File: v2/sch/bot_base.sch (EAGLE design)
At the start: 35 parts, among them K1 SKQGADE010, Q0 QWIIC_RIGHT_ANGLE, U1 ESP32-C3-MINI-1-N4, U2 AP7370-33SA (or MCP1703T-3302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, U4 LGS4084HB5

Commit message: routing almost finished
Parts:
- removed JUMPER_LIPO_CHG: NO-FIT, solder_jumper:WIRELINK2
- removed K1: SKQGADE010, Seeed-OPL-Button:SMD-SWITCH-TOP-260GF(4P-D5.2MM)
- added K2: DTSM-62K-S-V-T/R, Seeed-OPL-Button:SMD-SWITCH-TACTILE-SPST-NO(4P-D6.0MM)
- added R10: 10k, rcl:R-EU_R0603
- added SERVO: (no value), pinhead-2:PINHD-1X03_2.54-S
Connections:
- removed net N$2: JUMPER_LIPO_CHG.1, U4.BAT
- removed net N$7: K1.A0, U1.IO9
- new net BOOT: K2.A0, U1.IO9
- new net MOTOR1A_LV: U$3.INA, U1.IO4
- new net MOTOR1B_LV: U$3.INB, U1.IO7
- new net MOTOR2A_LV: U$4.INA, U1.IO6
- new net MOTOR2B_LV: U$4.INB, U1.IO5
- net +5V: now also SERVO.2, U$9.P$1
- net BUTTONS: now also R10.2
- net GND: now also C3.1, C4.1, K2.B0, SERVO.1, U$5.4; no longer K1.B0
- net MOTOR1A: now also U$3.OUTA, U$6.P$2; no longer U$3.INA, U$6.P$1, U1.IO4
- net MOTOR1B: now also U$3.OUTB, U$6.P$1; no longer U$3.INB, U$6.P$2, U1.IO7
- net MOTOR2A: now also U$4.OUTA, U$7.P$2; no longer U$4.INA, U$7.P$1, U1.IO6
- net MOTOR2B: now also U$4.OUTB, U$7.P$1; no longer U$4.INB, U$7.P$2, U1.IO5
- net TXD0_GPIO21: now also SERVO.3
- net VBAT: now also U$5.1, U4.BAT; no longer JUMPER_LIPO_CHG.2
- net VCC: now also R10.1; no longer U$9.P$1
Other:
- moved on the sheet: C4

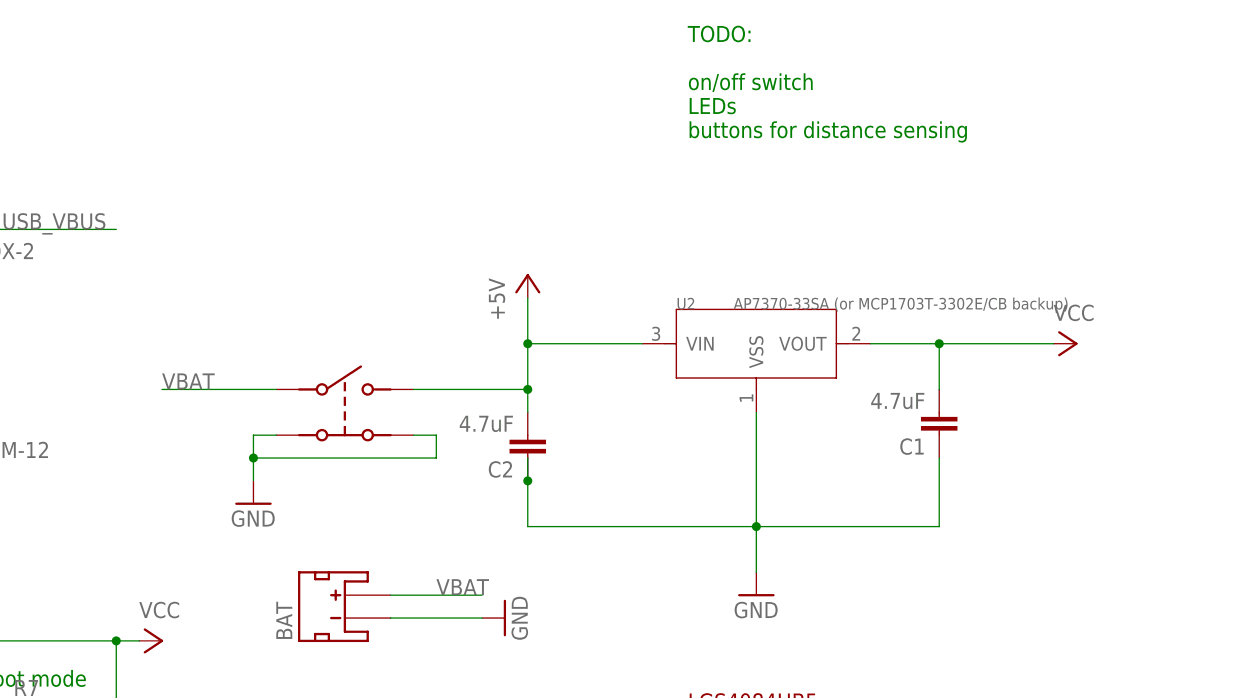
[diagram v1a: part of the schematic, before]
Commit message: switch update
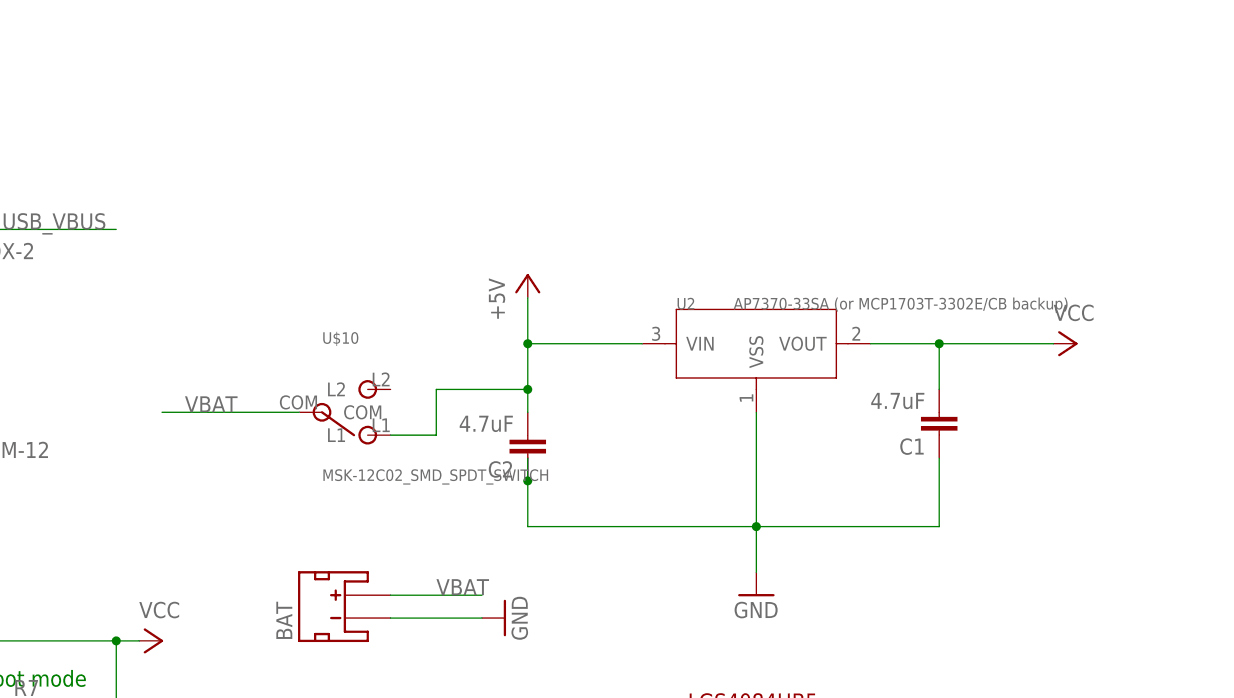
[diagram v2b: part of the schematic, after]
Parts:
- removed U$5: LY-SK-03, pimoroni-mechanical:LY-SK-03
- added U$10: MSK-12C02_SMD_SPDT_SWITCH, switch-MSK-12C02:MSK-12C02_SMD_SPDT_SWITCH
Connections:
- net +5V: now also U$10.L1; no longer U$5.3
- net GND: no longer U$5.2, U$5.4
- net VBAT: now also U$10.COM; no longer U$5.1
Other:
- note removed: "TODO: on/off switch LEDs buttons for distance sensing"
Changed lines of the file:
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@@
 <part name="F1" library="rcl" deviceset="R-EU_" device="R0603" value="MF-FSMF050X-2"/>
 <part name="P+7" library="supply1" deviceset="VCC" device=""/>
-<part name="U$5" library="pimoroni-mechanical" deviceset="LY-SK-03" device=""/>
-<part name="GND14" library="supply1" deviceset="GND" device=""/>
 <part name="LED2" library="led" deviceset="LED" device="CHIPLED_0603" value="RED"/>
 <part name="R3" library="rcl" deviceset="R-EU_" device="R0603" value="1K"/>
@@
 <part name="P+15" library="supply1" deviceset="+5V" device=""/>
 <part name="K2" library="Seeed-OPL-Button" deviceset="SMD-SWITCH-TACTILE-SPST-NO(4P-D6.0MM)" device="" value="DTSM-62K-S-V-T/R"/>
+<part name="U$10" library="switch-MSK-12C02" deviceset="MSK-12C02_SMD_SPDT_SWITCH" device=""/>
 </parts>
 <sheets>
@@
 <plain>
 <text x="139.7" y="91.44" size="1.778" layer="94">LGS4084HB5</text>
-<text x="139.7" y="154.94" size="1.778" layer="91">TODO:
-on/off switch
-LEDs
-buttons for distance sensing</text>
 <text x="-22.86" y="81.28" size="1.778" layer="91">Boot mode</text>
 <text x="60.96" y="93.98" size="1.778" layer="91">Boot mode</text>
@@
 <instance part="F1" gate="G$1" x="53.34" y="144.78"/>
 <instance part="P+7" gate="VCC" x="0" y="96.52" rot="R90"/>
-<instance part="U$5" gate="G$1" x="116.84" y="119.38"/>
-<instance part="GND14" gate="1" x="91.44" y="114.3"/>
 <instance part="LED2" gate="G$1" x="58.42" y="88.9" rot="R270"/>
 <instance part="R3" gate="G$1" x="68.58" y="88.9" rot="R180"/>
@@
 <instance part="P+15" gate="1" x="-27.94" y="66.04" rot="R270"/>
 <instance part="K2" gate="G$1" x="90.17" y="83.82"/>
+<instance part="U$10" gate="MSK-12C02" x="104.14" y="124.46"/>
 </instances>
 <busses>
@@
 </segment>
 <segment>
-<pinref part="U$5" gate="G$1" pin="2"/>
-<wire x1="93.98" y1="121.92" x2="91.44" y2="121.92" width="0.1524" layer="91"/>
-<wire x1="91.44" y1="121.92" x2="91.44" y2="119.38" width="0.1524" layer="91"/>
-<pinref part="GND14" gate="1" pin="GND"/>
-<pinref part="U$5" gate="G$1" pin="4"/>
-<wire x1="91.44" y1="119.38" x2="91.44" y2="116.84" width="0.1524" layer="91"/>
-<wire x1="109.22" y1="121.92" x2="111.76" y2="121.92" width="0.1524" layer="91"/>
-<wire x1="111.76" y1="121.92" x2="111.76" y2="119.38" width="0.1524" layer="91"/>
-<wire x1="111.76" y1="119.38" x2="91.44" y2="119.38" width="0.1524" layer="91"/>
-<junction x="91.44" y="119.38"/>
-</segment>
-<segment>
 <label x="-30.48" y="33.02" size="1.778" layer="95"/>
 <pinref part="Q0" gate="J1" pin="1"/>
@@
 </segment>
 <segment>
-<wire x1="93.98" y1="127" x2="81.28" y2="127" width="0.1524" layer="91"/>
-<label x="81.28" y="127" size="1.778" layer="95"/>
-<pinref part="U$5" gate="G$1" pin="1"/>
+<label x="83.82" y="124.46" size="1.778" layer="95"/>
+<pinref part="U$10" gate="MSK-12C02" pin="COM"/>
+<wire x1="81.28" y1="124.46" x2="96.52" y2="124.46" width="0.1524" layer="91"/>
 </segment>
 </net>
@@
 <wire x1="121.92" y1="124.46" x2="121.92" y2="127" width="0.1524" layer="91"/>
 <wire x1="121.92" y1="127" x2="121.92" y2="132.08" width="0.1524" layer="91"/>
-<wire x1="109.22" y1="127" x2="121.92" y2="127" width="0.1524" layer="91"/>
 <junction x="121.92" y="127"/>
 <pinref part="C2" gate="G$1" pin="2"/>
 <pinref part="P+1" gate="1" pin="+5V"/>
-<pinref part="U$5" gate="G$1" pin="3"/>
+<pinref part="U$10" gate="MSK-12C02" pin="L1"/>
+<wire x1="111.76" y1="127" x2="121.92" y2="127" width="0.1524" layer="91"/>
+<wire x1="106.68" y1="121.92" x2="111.76" y2="121.92" width="0.1524" layer="91"/>
+<wire x1="111.76" y1="121.92" x2="111.76" y2="127" width="0.1524" layer="91"/>
 </segment>
 <segment>
@@
 </schematic>
 </drawing>
-<compatibility>
-<note version="6.3" minversion="6.2.2" severity="warning">
-Since Version 6.2.2 text objects can contain more than one line,
-which will not be processed correctly with this version.
-</note>
-</compatibility>
 </eagle>

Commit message: mid-update, fixing issues
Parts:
- added LED3: RED, led:LEDCHIPLED_0603
- added R13: 10k, rcl:R-EU_R0603
- R4, R5: value 300 -> 100
- U$1, U$2: value XL-ITR9608 -> XL-ITR9707; device ir-XINGLIGHT-XL-ITR9608:XL-ITR9608 -> ir-XINGLIGHT-XL-ITR9608:XL-ITR9707
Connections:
- new net N$2: LED3.C, R13.2
- net GND: now also R13.1
- net VCC: now also LED3.A
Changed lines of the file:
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@@
 </classes>
 <parts>
-<part name="U$1" library="ir-XINGLIGHT-XL-ITR9608" deviceset="XL-ITR9608" device=""/>
-<part name="U$2" library="ir-XINGLIGHT-XL-ITR9608" deviceset="XL-ITR9608" device=""/>
+<part name="U$1" library="ir-XINGLIGHT-XL-ITR9608" deviceset="XL-ITR9707" device=""/>
+<part name="U$2" library="ir-XINGLIGHT-XL-ITR9608" deviceset="XL-ITR9707" device=""/>
 <part name="GND1" library="supply1" deviceset="GND" device=""/>
 <part name="GND3" library="supply1" deviceset="GND" device=""/>
@@
 <part name="LED2" library="led" deviceset="LED" device="CHIPLED_0603" value="RED"/>
 <part name="R3" library="rcl" deviceset="R-EU_" device="R0603" value="1K"/>
-<part name="R4" library="rcl" deviceset="R-EU_" device="R0603" value="300"/>
-<part name="R5" library="rcl" deviceset="R-EU_" device="R0603" value="300"/>
+<part name="R4" library="rcl" deviceset="R-EU_" device="R0603" value="100"/>
+<part name="R5" library="rcl" deviceset="R-EU_" device="R0603" value="100"/>
 <part name="R6" library="rcl" deviceset="R-EU_" device="R0603" value="10k"/>
 <part name="P+6" library="supply1" deviceset="VCC" device=""/>
@@
 <part name="K2" library="Seeed-OPL-Button" deviceset="SMD-SWITCH-TACTILE-SPST-NO(4P-D6.0MM)" device="" value="DTSM-62K-S-V-T/R"/>
 <part name="U$10" library="switch-MSK-12C02" deviceset="MSK-12C02_SMD_SPDT_SWITCH" device=""/>
+<part name="LED3" library="led" deviceset="LED" device="CHIPLED_0603" value="RED"/>
+<part name="R13" library="rcl" deviceset="R-EU_" device="R0603" value="10k"/>
 </parts>
 <sheets>
@@
 <instance part="K2" gate="G$1" x="90.17" y="83.82"/>
 <instance part="U$10" gate="MSK-12C02" x="104.14" y="124.46"/>
+<instance part="LED3" gate="G$1" x="175.26" y="124.46"/>
+<instance part="R13" gate="G$1" x="175.26" y="111.76" rot="R90"/>
 </instances>
 <busses>
@@
 <wire x1="121.92" y1="116.84" x2="121.92" y2="111.76" width="0.1524" layer="91"/>
 <junction x="121.92" y="116.84"/>
+<pinref part="R13" gate="G$1" pin="1"/>
+<wire x1="175.26" y1="106.68" x2="175.26" y2="104.14" width="0.1524" layer="91"/>
+<wire x1="175.26" y1="104.14" x2="167.64" y2="104.14" width="0.1524" layer="91"/>
+<wire x1="167.64" y1="104.14" x2="167.64" y2="111.76" width="0.1524" layer="91"/>
+<junction x="167.64" y="111.76"/>
 </segment>
 <segment>
@@
 <pinref part="P+3" gate="VCC" pin="VCC"/>
 <pinref part="C1" gate="G$1" pin="2"/>
-<wire x1="167.64" y1="132.08" x2="180.34" y2="132.08" width="0.1524" layer="91"/>
+<wire x1="167.64" y1="132.08" x2="175.26" y2="132.08" width="0.1524" layer="91"/>
+<wire x1="175.26" y1="132.08" x2="180.34" y2="132.08" width="0.1524" layer="91"/>
 <wire x1="167.64" y1="127" x2="167.64" y2="132.08" width="0.1524" layer="91"/>
 <junction x="167.64" y="132.08"/>
 <pinref part="U2" gate="G$1" pin="VOUT"/>
 <wire x1="167.64" y1="132.08" x2="160.02" y2="132.08" width="0.1524" layer="91"/>
+<pinref part="LED3" gate="G$1" pin="A"/>
+<wire x1="175.26" y1="132.08" x2="175.26" y2="127" width="0.1524" layer="91"/>
+<junction x="175.26" y="132.08"/>
 </segment>
 <segment>
@@
 </segment>
 </net>
+<net name="N$2" class="0">
+<segment>
+<pinref part="LED3" gate="G$1" pin="C"/>
+<pinref part="R13" gate="G$1" pin="2"/>
+<wire x1="175.26" y1="119.38" x2="175.26" y2="116.84" width="0.1524" layer="91"/>
+</segment>
+</net>

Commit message: latest relayout
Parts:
- removed U2: AP7370-33SA (or MCP1703T-3302E/CB backup), mcp1703t:MCP1703T
- added C5: 4.7uF, rcl:C-EUC0805
- added U$5: AP7361C-33E-13, vreg:AP7361C-33E-13
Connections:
- net +5V: now also LED3.A, U$5.VIN; no longer C2.2, U2.VIN
- net GND: now also C5.1, U$5.VSS; no longer U2.VSS
- net VBAT: now also C2.2
- net VCC: now also C5.2, U$5.VOUT; no longer LED3.A, U2.VOUT
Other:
- moved on the sheet: C2, LED3, R13
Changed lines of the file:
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@@
 <setting verticaltext="up"/>
 </settings>
-<grid distance="0.1" unitdist="inch" unit="inch" style="lines" multiple="1" display="no" altdistance="0.01" altunitdist="inch" altunit="inch"/>
+<grid distance="0.05" unitdist="inch" unit="inch" style="lines" multiple="1" display="no" altdistance="0.01" altunitdist="inch" altunit="inch"/>
 <layers>
 <layer number="1" name="Top" color="4" fill="1" visible="no" active="no"/>
@@
 <part name="GND10" library="supply1" deviceset="GND" device=""/>
 <part name="P+3" library="supply1" deviceset="VCC" device=""/>
-<part name="U2" library="mcp1703t" deviceset="MCP1703T" device="" value="AP7370-33SA (or MCP1703T-3302E/CB backup)"/>
 <part name="BAT" library="SparkFun-Connectors" deviceset="JST_2MM_MALE" device="" value="C47647 / S2B-PH-SM4-TB"/>
 <part name="GND12" library="supply1" deviceset="GND" device=""/>
@@
 <part name="LED3" library="led" deviceset="LED" device="CHIPLED_0603" value="RED"/>
 <part name="R13" library="rcl" deviceset="R-EU_" device="R0603" value="10k"/>
+<part name="GND14" library="supply1" deviceset="GND" device=""/>
+<part name="U$5" library="vreg" deviceset="AP7361C-33E-13" device=""/>
+<part name="C5" library="rcl" deviceset="C-EU" device="C0805" value="4.7uF"/>
 </parts>
 <sheets>
@@
 <instance part="LED1" gate="G$1" x="172.72" y="83.82" rot="R270"/>
 <instance part="C1" gate="G$1" x="167.64" y="121.92" rot="R180"/>
-<instance part="GND10" gate="1" x="147.32" y="104.14"/>
+<instance part="GND10" gate="1" x="147.32" y="99.06"/>
 <instance part="P+3" gate="VCC" x="182.88" y="132.08" rot="R270"/>
-<instance part="U2" gate="G$1" x="147.32" y="132.08"/>
 <instance part="BAT" gate="G$1" x="101.6" y="101.6" rot="R90"/>
 <instance part="GND12" gate="1" x="119.38" y="101.6" rot="R90"/>
-<instance part="C2" gate="G$1" x="121.92" y="119.38" rot="R180"/>
+<instance part="C2" gate="G$1" x="91.44" y="116.84" rot="R180"/>
 <instance part="C3" gate="G$1" x="38.1" y="-20.32" rot="R180"/>
 <instance part="C4" gate="G$1" x="38.1" y="5.08" rot="R180"/>
-<instance part="P+1" gate="1" x="121.92" y="139.7"/>
+<instance part="P+1" gate="1" x="129.54" y="137.16"/>
 <instance part="P+2" gate="1" x="38.1" y="17.78"/>
 <instance part="P+4" gate="1" x="38.1" y="-7.62"/>
@@
 <instance part="K2" gate="G$1" x="90.17" y="83.82"/>
 <instance part="U$10" gate="MSK-12C02" x="104.14" y="124.46"/>
-<instance part="LED3" gate="G$1" x="175.26" y="124.46"/>
-<instance part="R13" gate="G$1" x="175.26" y="111.76" rot="R90"/>
+<instance part="LED3" gate="G$1" x="129.54" y="127"/>
+<instance part="R13" gate="G$1" x="129.54" y="114.3" rot="R90"/>
+<instance part="GND14" gate="1" x="91.44" y="109.22"/>
+<instance part="U$5" gate="G$1" x="147.32" y="132.08"/>
+<instance part="C5" gate="G$1" x="173.99" y="121.92" rot="R180"/>
 </instances>
 <busses>
@@
 </segment>
 <segment>
-<pinref part="GND10" gate="1" pin="GND"/>
-<wire x1="147.32" y1="111.76" x2="147.32" y2="106.68" width="0.1524" layer="91"/>
-<wire x1="121.92" y1="111.76" x2="147.32" y2="111.76" width="0.1524" layer="91"/>
-<pinref part="C1" gate="G$1" pin="1"/>
-<wire x1="147.32" y1="111.76" x2="167.64" y2="111.76" width="0.1524" layer="91"/>
-<wire x1="167.64" y1="111.76" x2="167.64" y2="119.38" width="0.1524" layer="91"/>
-<junction x="147.32" y="111.76"/>
-<wire x1="147.32" y1="124.46" x2="147.32" y2="111.76" width="0.1524" layer="91"/>
-<pinref part="U2" gate="G$1" pin="VSS"/>
-<wire x1="121.92" y1="119.38" x2="121.92" y2="116.84" width="0.1524" layer="91"/>
-<pinref part="C2" gate="G$1" pin="1"/>
-<wire x1="121.92" y1="116.84" x2="121.92" y2="111.76" width="0.1524" layer="91"/>
-<junction x="121.92" y="116.84"/>
-<pinref part="R13" gate="G$1" pin="1"/>
-<wire x1="175.26" y1="106.68" x2="175.26" y2="104.14" width="0.1524" layer="91"/>
-<wire x1="175.26" y1="104.14" x2="167.64" y2="104.14" width="0.1524" layer="91"/>
-<wire x1="167.64" y1="104.14" x2="167.64" y2="111.76" width="0.1524" layer="91"/>
-<junction x="167.64" y="111.76"/>
-</segment>
-<segment>
 <pinref part="BAT" gate="G$1" pin="-"/>
 <pinref part="GND12" gate="1" pin="GND"/>
@@
 <pinref part="GND13" gate="1" pin="GND"/>
 </segment>
+<segment>
+<wire x1="91.44" y1="111.76" x2="91.44" y2="114.3" width="0.1524" layer="91"/>
+<pinref part="C2" gate="G$1" pin="1"/>
+<pinref part="GND14" gate="1" pin="GND"/>
+</segment>
+<segment>
+<pinref part="GND10" gate="1" pin="GND"/>
+<wire x1="147.32" y1="106.68" x2="147.32" y2="101.6" width="0.1524" layer="91"/>
+<pinref part="C1" gate="G$1" pin="1"/>
+<wire x1="129.54" y1="106.68" x2="147.32" y2="106.68" width="0.1524" layer="91"/>
+<wire x1="147.32" y1="106.68" x2="167.64" y2="106.68" width="0.1524" layer="91"/>
+<wire x1="167.64" y1="106.68" x2="167.64" y2="119.38" width="0.1524" layer="91"/>
+<junction x="147.32" y="106.68"/>
+<wire x1="147.32" y1="124.46" x2="147.32" y2="106.68" width="0.1524" layer="91"/>
+<pinref part="R13" gate="G$1" pin="1"/>
+<wire x1="129.54" y1="109.22" x2="129.54" y2="106.68" width="0.1524" layer="91"/>
+<pinref part="U$5" gate="G$1" pin="VSS"/>
+<pinref part="C5" gate="G$1" pin="1"/>
+<wire x1="173.99" y1="119.38" x2="173.99" y2="106.68" width="0.1524" layer="91"/>
+<wire x1="173.99" y1="106.68" x2="167.64" y2="106.68" width="0.1524" layer="91"/>
+<junction x="167.64" y="106.68"/>
+</segment>
 </net>
 <net name="MOTOR1A" class="0">
@@
 <label x="83.82" y="124.46" size="1.778" layer="95"/>
 <pinref part="U$10" gate="MSK-12C02" pin="COM"/>
-<wire x1="81.28" y1="124.46" x2="96.52" y2="124.46" width="0.1524" layer="91"/>
+<wire x1="81.28" y1="124.46" x2="91.44" y2="124.46" width="0.1524" layer="91"/>
+<pinref part="C2" gate="G$1" pin="2"/>
+<wire x1="91.44" y1="124.46" x2="96.52" y2="124.46" width="0.1524" layer="91"/>
+<wire x1="91.44" y1="121.92" x2="91.44" y2="124.46" width="0.1524" layer="91"/>
+<junction x="91.44" y="124.46"/>
 </segment>
 </net>
@@
 <pinref part="P+3" gate="VCC" pin="VCC"/>
 <pinref part="C1" gate="G$1" pin="2"/>
-<wire x1="167.64" y1="132.08" x2="175.26" y2="132.08" width="0.1524" layer="91"/>
-<wire x1="175.26" y1="132.08" x2="180.34" y2="132.08" width="0.1524" layer="91"/>
+<wire x1="167.64" y1="132.08" x2="173.99" y2="132.08" width="0.1524" layer="91"/>
+<wire x1="173.99" y1="132.08" x2="180.34" y2="132.08" width="0.1524" layer="91"/>
 <wire x1="167.64" y1="127" x2="167.64" y2="132.08" width="0.1524" layer="91"/>
 <junction x="167.64" y="132.08"/>
-<pinref part="U2" gate="G$1" pin="VOUT"/>
 <wire x1="167.64" y1="132.08" x2="160.02" y2="132.08" width="0.1524" layer="91"/>
-<pinref part="LED3" gate="G$1" pin="A"/>
-<wire x1="175.26" y1="132.08" x2="175.26" y2="127" width="0.1524" layer="91"/>
-<junction x="175.26" y="132.08"/>
+<pinref part="U$5" gate="G$1" pin="VOUT"/>
+<pinref part="C5" gate="G$1" pin="2"/>
+<wire x1="173.99" y1="132.08" x2="173.99" y2="127" width="0.1524" layer="91"/>
+<junction x="173.99" y="132.08"/>
 </segment>
 <segment>
@@
 <net name="+5V" class="0">
 <segment>
-<wire x1="134.62" y1="132.08" x2="121.92" y2="132.08" width="0.1524" layer="91"/>
-<wire x1="121.92" y1="132.08" x2="121.92" y2="137.16" width="0.1524" layer="91"/>
-<pinref part="U2" gate="G$1" pin="VIN"/>
-<junction x="121.92" y="132.08"/>
-<wire x1="121.92" y1="124.46" x2="121.92" y2="127" width="0.1524" layer="91"/>
-<wire x1="121.92" y1="127" x2="121.92" y2="132.08" width="0.1524" layer="91"/>
-<junction x="121.92" y="127"/>
-<pinref part="C2" gate="G$1" pin="2"/>
+<wire x1="134.62" y1="132.08" x2="129.54" y2="132.08" width="0.1524" layer="91"/>
+<wire x1="129.54" y1="132.08" x2="129.54" y2="134.62" width="0.1524" layer="91"/>
+<junction x="129.54" y="132.08"/>
 <pinref part="P+1" gate="1" pin="+5V"/>
 <pinref part="U$10" gate="MSK-12C02" pin="L1"/>
-<wire x1="111.76" y1="127" x2="121.92" y2="127" width="0.1524" layer="91"/>
+<wire x1="111.76" y1="132.08" x2="129.54" y2="132.08" width="0.1524" layer="91"/>
 <wire x1="106.68" y1="121.92" x2="111.76" y2="121.92" width="0.1524" layer="91"/>
-<wire x1="111.76" y1="121.92" x2="111.76" y2="127" width="0.1524" layer="91"/>
+<wire x1="111.76" y1="121.92" x2="111.76" y2="132.08" width="0.1524" layer="91"/>
+<pinref part="LED3" gate="G$1" pin="A"/>
+<wire x1="129.54" y1="129.54" x2="129.54" y2="132.08" width="0.1524" layer="91"/>
+<pinref part="U$5" gate="G$1" pin="VIN"/>
 </segment>
 <segment>
@@
 <pinref part="LED3" gate="G$1" pin="C"/>
 <pinref part="R13" gate="G$1" pin="2"/>
-<wire x1="175.26" y1="119.38" x2="175.26" y2="116.84" width="0.1524" layer="91"/>
-</segment>
-</net>
+<wire x1="129.54" y1="121.92" x2="129.54" y2="119.38" width="0.1524" layer="91"/>
+</segment>
+</net>
